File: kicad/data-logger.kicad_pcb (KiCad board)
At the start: 2 copper layers, 37 x 46 mm, 35 parts, among them M1 M50-3130545, P1 PI4ULS3V501TAEX, P2 PI4ULS3V501TAEX, P3 PI4ULS3V501TAEX, P4 PI4ULS3V501TAEX, SW1 SW_Push, T1 TLV61225DCKR, U1 DMP2008UFG-7, Y1 32.768 kHz

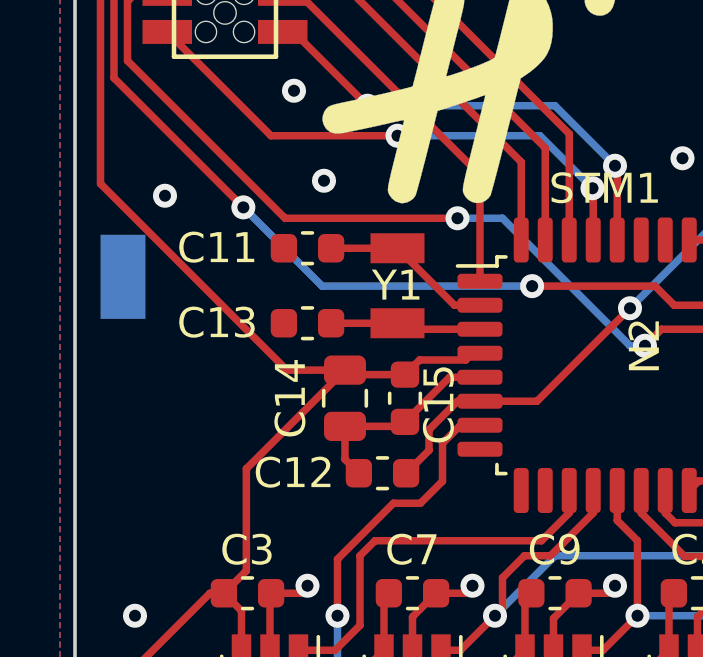
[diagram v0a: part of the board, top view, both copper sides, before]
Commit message: switched the size of C14
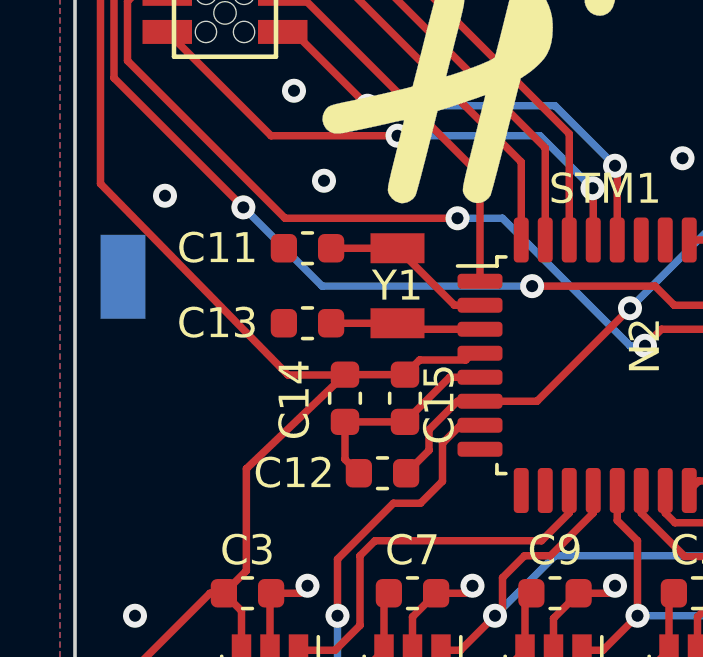
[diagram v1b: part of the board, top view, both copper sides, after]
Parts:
- C14: footprint Capacitor_SMD:C_0805_2012Metric -> Capacitor_SMD:C_0603_1608Metric
